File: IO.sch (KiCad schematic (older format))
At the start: 22 parts, among them SW2 CH1_Vadj, SW3 CH2_Vadj, U5 74HC14, U6 MCP23008-xP, U7 4013

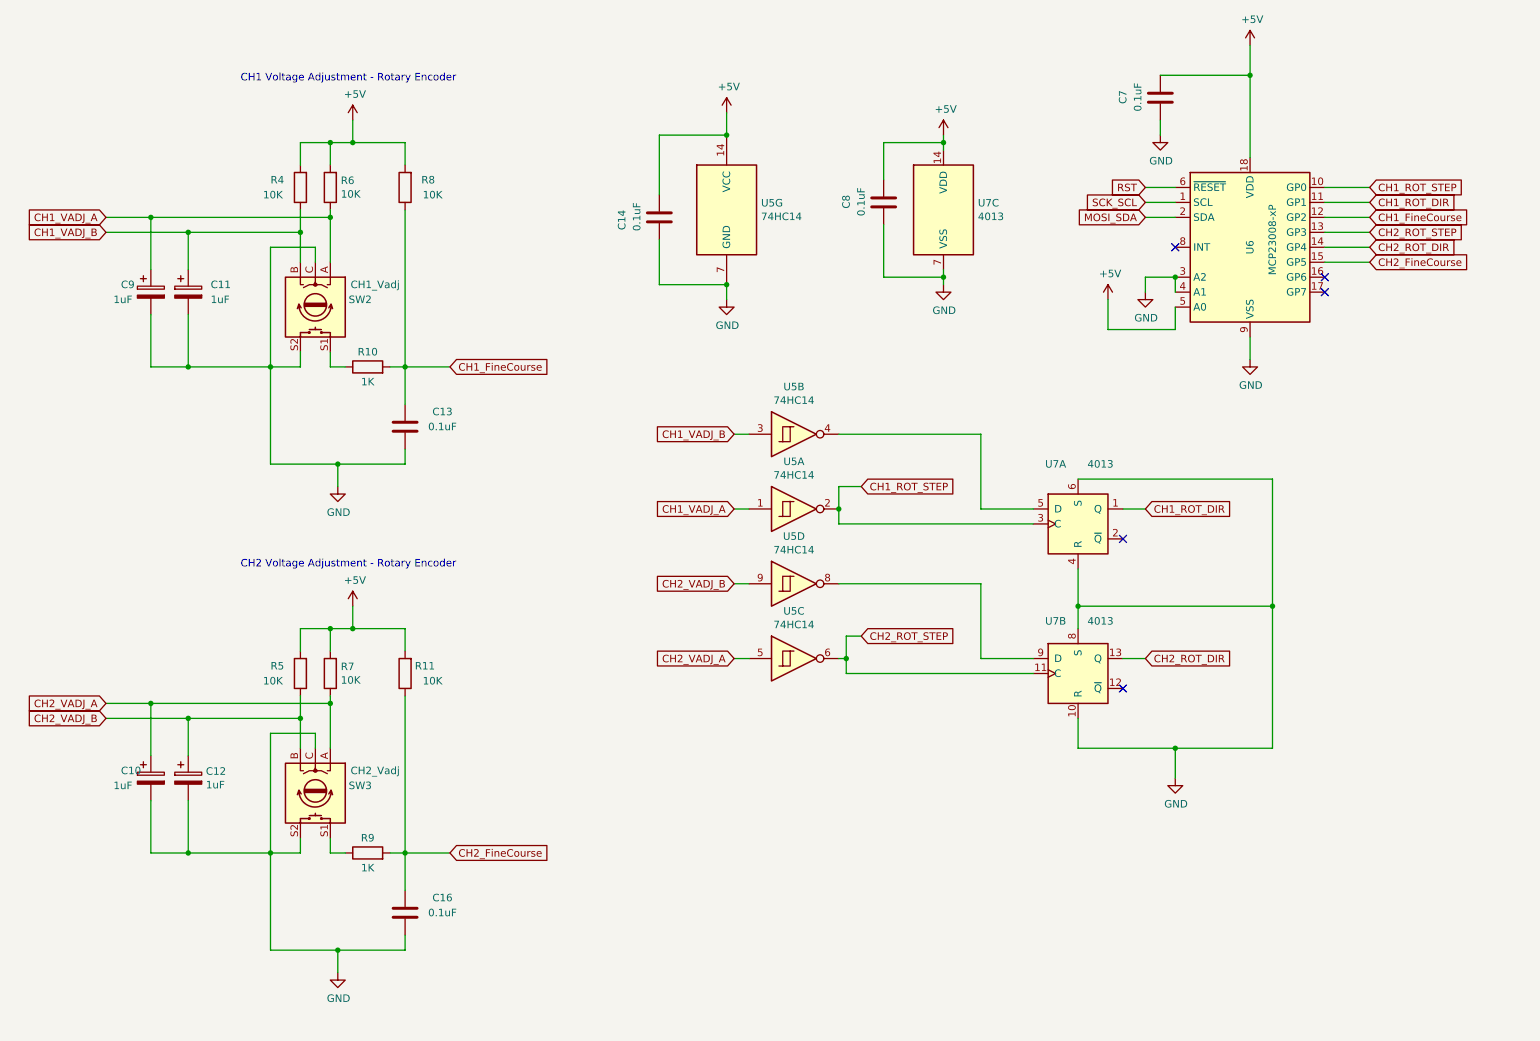
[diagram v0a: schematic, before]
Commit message: Switched the MCU to a basic STM32, changed the business logic to 3V3, created a new 3V3 regulator for this. Also initialised code base. We'll use ARM Mbed for rapid development
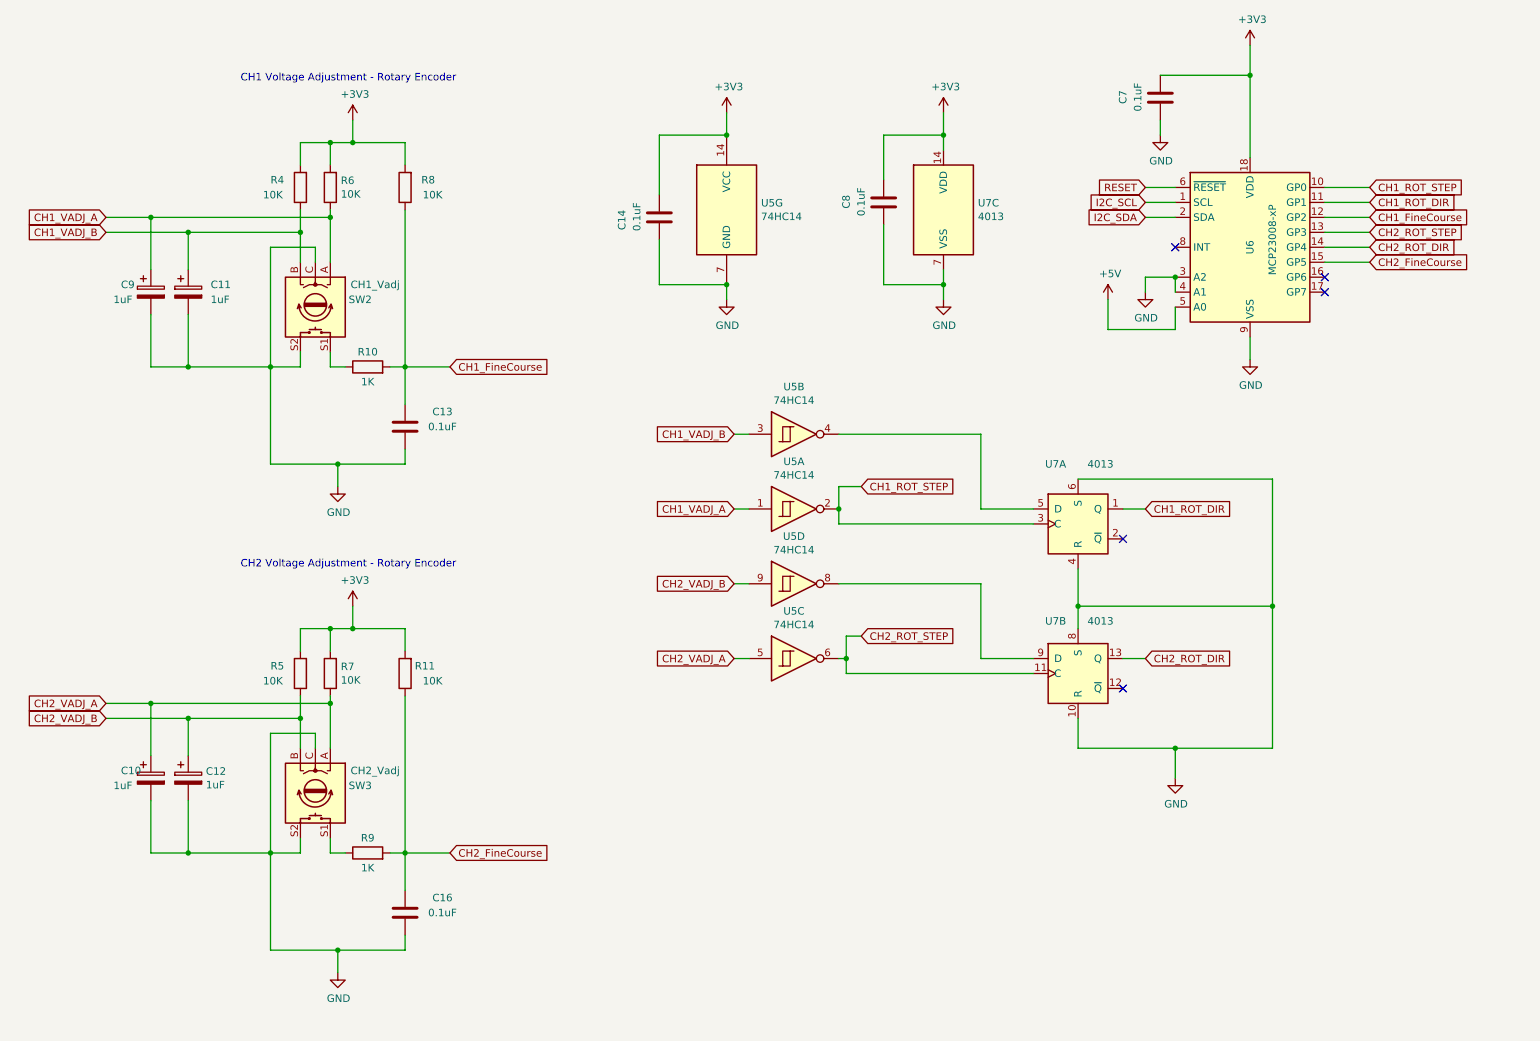
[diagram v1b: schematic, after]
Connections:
- net +5V: no longer C14.2, C7.2, C8.2, R11.2, R4.2, R5.2, R6.2, R7.2, R8.2, U5.14 (VCC), U6.18 (VDD), U7.14 (VDD)
- net MOSI_SDA renamed I2C_SDA
- net RST renamed RESET
- net SCK_SCL renamed I2C_SCL
- new net +3V3: C14.2, C7.2, C8.2, R11.2, R4.2, R5.2, R6.2, R7.2, R8.2, U5.14 (VCC), U6.18 (VDD), U7.14 (VDD)
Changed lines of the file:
@@
 	1    0    0    -1
 $EndComp
-Text GLabel 8300 1850 0    50   Input ~ 0
-RST
 Wire Wire Line
 	8500 1850 8300 1850
-Text GLabel 8300 1950 0    50   Input ~ 0
-SCK_SCL
-Text GLabel 8300 2050 0    50   Input ~ 0
-MOSI_SDA
 Wire Wire Line
 	8500 1950 8300 1950
@@
 	9000 1100 9000 900
 Connection ~ 9000 1100
-$Comp
-L power:+5V #PWR?
-U 1 1 60565429
-P 9000 900
-AR Path="/60565429" Ref="#PWR?"  Part="1"
-AR Path="/604E5285/60565429" Ref="#PWR0119"  Part="1"
-F 0 "#PWR0119" H 9000 750 50  0001 C CNN
-F 1 "+5V" H 9015 1073 50  0000 C CNN
-F 2 "" H 9000 900 50  0001 C CNN
-F 3 "" H 9000 900 50  0001 C CNN
-	1    9000 900
-	1    0    0    -1
-$EndComp
 Wire Wire Line
 	9500 1850 9800 1850
@@
 Wire Wire Line
 	9500 2350 9800 2350
-$Comp
-L power:+5V #PWR?
-U 1 1 605B59EA
-P 3000 1400
-AR Path="/605B59EA" Ref="#PWR?"  Part="1"
-AR Path="/604E5285/605B59EA" Ref="#PWR0121"  Part="1"
-F 0 "#PWR0121" H 3000 1250 50  0001 C CNN
-F 1 "+5V" H 3015 1573 50  0000 C CNN
-F 2 "" H 3000 1400 50  0001 C CNN
-F 3 "" H 3000 1400 50  0001 C CNN
-	1    3000 1400
-	1    0    0    -1
-$EndComp
 $Comp
 L Device:R R?
@@
 	1    0    0    -1
 $EndComp
-$Comp
-L 4xxx:4013 U?
-U 3 1 605B5AC9
-P 6950 2000
-AR Path="/605B5AC9" Ref="U?"  Part="3"
-AR Path="/604E5285/605B5AC9" Ref="U7"  Part="3"
-F 0 "U7" H 7180 2046 50  0000 L CNN
-F 1 "4013" H 7180 1955 50  0000 L CNN
-F 2 "" H 6950 2000 50  0001 C CNN
-F 3 "http://www.onsemi.com/pub/Collateral/MC14013B-D.PDF" H 6950 2000 50  0001 C CNN
-	3    6950 2000
-	1    0    0    -1
-$EndComp
 Text Notes 2250 1150 0    50   ~ 0
 CH1 Voltage Adjustment - Rotary Encoder\n
 $Comp
-L power:+5V #PWR?
-U 1 1 605B5AD1
-P 6950 1500
-AR Path="/605B5AD1" Ref="#PWR?"  Part="1"
-AR Path="/604E5285/605B5AD1" Ref="#PWR0124"  Part="1"
-F 0 "#PWR0124" H 6950 1350 50  0001 C CNN
-F 1 "+5V" H 6965 1673 50  0000 C CNN
-F 2 "" H 6950 1500 50  0001 C CNN
-F 3 "" H 6950 1500 50  0001 C CNN
-	1    6950 1500
-	1    0    0    -1
-$EndComp
-Wire Wire Line
-	6950 1500 6950 1550
-$Comp
 L power:GND #PWR?
 U 1 1 605B5AD8
-P 6950 2500
+P 6950 2600
 AR Path="/605B5AD8" Ref="#PWR?"  Part="1"
 AR Path="/604E5285/605B5AD8" Ref="#PWR0125"  Part="1"
-F 0 "#PWR0125" H 6950 2250 50  0001 C CNN
-F 1 "GND" H 6955 2327 50  0000 C CNN
-F 2 "" H 6950 2500 50  0001 C CNN
-F 3 "" H 6950 2500 50  0001 C CNN
-	1    6950 2500
-	1    0    0    -1
-$EndComp
-Wire Wire Line
-	6950 2400 6950 2450
+F 0 "#PWR0125" H 6950 2350 50  0001 C CNN
+F 1 "GND" H 6955 2427 50  0000 C CNN
+F 2 "" H 6950 2600 50  0001 C CNN
+F 3 "" H 6950 2600 50  0001 C CNN
+	1    6950 2600
+	1    0    0    -1
+$EndComp
 $Comp
 L Device:C C?
@@
 	-1   0    0    1
 $EndComp
-Wire Wire Line
-	6550 1550 6950 1550
-Connection ~ 6950 1550
-Wire Wire Line
-	6950 1550 6950 1600
-Wire Wire Line
-	6550 2450 6950 2450
-Connection ~ 6950 2450
-Wire Wire Line
-	6950 2450 6950 2500
-Wire Wire Line
-	6550 1800 6550 1550
-Wire Wire Line
-	6550 2100 6550 2450
 $Comp
 L 74xx:74HC14 U?
@@
 Wire Wire Line
 	2850 1550 3000 1550
-Wire Wire Line
-	3000 1550 3000 1400
 Connection ~ 3000 1550
 Wire Wire Line
@@
 Text GLabel 1350 2150 0    50   Input ~ 0
 CH1_VADJ_B
-$Comp
-L power:+5V #PWR?
-U 1 1 606CCC08
-P 3000 4650
-AR Path="/606CCC08" Ref="#PWR?"  Part="1"
-AR Path="/604E5285/606CCC08" Ref="#PWR04"  Part="1"
-F 0 "#PWR04" H 3000 4500 50  0001 C CNN
-F 1 "+5V" H 3015 4823 50  0000 C CNN
-F 2 "" H 3000 4650 50  0001 C CNN
-F 3 "" H 3000 4650 50  0001 C CNN
-	1    3000 4650
-	1    0    0    -1
-$EndComp
 $Comp
 L Device:R R?
@@
 	1    5050 2050
 	-1   0    0    1
-$EndComp
-$Comp
-L power:+5V #PWR?
-U 1 1 60790073
-P 5500 1350
-AR Path="/60790073" Ref="#PWR?"  Part="1"
-AR Path="/604E5285/60790073" Ref="#PWR09"  Part="1"
-F 0 "#PWR09" H 5500 1200 50  0001 C CNN
-F 1 "+5V" H 5515 1523 50  0000 C CNN
-F 2 "" H 5500 1350 50  0001 C CNN
-F 3 "" H 5500 1350 50  0001 C CNN
-	1    5500 1350
-	1    0    0    -1
 $EndComp
 $Comp
@@
 NoConn ~ 9500 2450
 NoConn ~ 9500 2550
+Text GLabel 8300 1950 0    50   Input ~ 0
+I2C_SCL
+Text GLabel 8300 2050 0    50   Input ~ 0
+I2C_SDA
+Text GLabel 8300 1850 0    50   Input ~ 0
+RESET
+$Comp
+L power:+3V3 #PWR?
+U 1 1 600ABCA0
+P 6950 1350
+F 0 "#PWR?" H 6950 1200 50  0001 C CNN
+F 1 "+3V3" H 6965 1523 50  0000 C CNN
+F 2 "" H 6950 1350 50  0001 C CNN
+F 3 "" H 6950 1350 50  0001 C CNN
+	1    6950 1350
+	1    0    0    -1
+$EndComp
+Wire Wire Line
+	6950 1500 6550 1500
+Wire Wire Line
+	6950 1350 6950 1500
+Wire Wire Line
+	6550 1500 6550 1800
+$Comp
+L 4xxx:4013 U?
+U 3 1 605B5AC9
+P 6950 2000
+AR Path="/605B5AC9" Ref="U?"  Part="3"
+AR Path="/604E5285/605B5AC9" Ref="U7"  Part="3"
+F 0 "U7" H 7180 2046 50  0000 L CNN
+F 1 "4013" H 7180 1955 50  0000 L CNN
+F 2 "" H 6950 2000 50  0001 C CNN
+F 3 "http://www.onsemi.com/pub/Collateral/MC14013B-D.PDF" H 6950 2000 50  0001 C CNN
+	3    6950 2000
+	1    0    0    -1
+$EndComp
+Wire Wire Line
+	6950 1600 6950 1500
+Connection ~ 6950 1500
+Wire Wire Line
+	6950 2400 6950 2500
+Wire Wire Line
+	6550 2500 6950 2500
+Wire Wire Line
+	6550 2100 6550 2500
+Connection ~ 6950 2500
+Wire Wire Line
+	6950 2500 6950 2600
+Wire Wire Line
+	3000 1550 3000 1400
+$Comp
+L power:+3V3 #PWR?
+U 1 1 600C9E7A
+P 3000 1400
+F 0 "#PWR?" H 3000 1250 50  0001 C CNN
+F 1 "+3V3" H 3015 1573 50  0000 C CNN
+F 2 "" H 3000 1400 50  0001 C CNN
+F 3 "" H 3000 1400 50  0001 C CNN
+	1    3000 1400
+	1    0    0    -1
+$EndComp
+$Comp
+L power:+3V3 #PWR?
+U 1 1 600CA50D
+P 5500 1350
+F 0 "#PWR?" H 5500 1200 50  0001 C CNN
+F 1 "+3V3" H 5515 1523 50  0000 C CNN
+F 2 "" H 5500 1350 50  0001 C CNN
+F 3 "" H 5500 1350 50  0001 C CNN
+	1    5500 1350
+	1    0    0    -1
+$EndComp
+$Comp
+L power:+3V3 #PWR?
+U 1 1 600CB0A8
+P 9000 900
+F 0 "#PWR?" H 9000 750 50  0001 C CNN
+F 1 "+3V3" H 9015 1073 50  0000 C CNN
+F 2 "" H 9000 900 50  0001 C CNN
+F 3 "" H 9000 900 50  0001 C CNN
+	1    9000 900
+	1    0    0    -1
+$EndComp
+$Comp
+L power:+3V3 #PWR?
+U 1 1 600CB5E9
+P 3000 4650
+F 0 "#PWR?" H 3000 4500 50  0001 C CNN
+F 1 "+3V3" H 3015 4823 50  0000 C CNN
+F 2 "" H 3000 4650 50  0001 C CNN
+F 3 "" H 3000 4650 50  0001 C CNN
+	1    3000 4650
+	1    0    0    -1
+$EndComp
 $EndSCHEMATC

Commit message: had to reload source files. Waiting on the STM32F01 so will compile for target STM32F303 for now. Just a temporary change for now
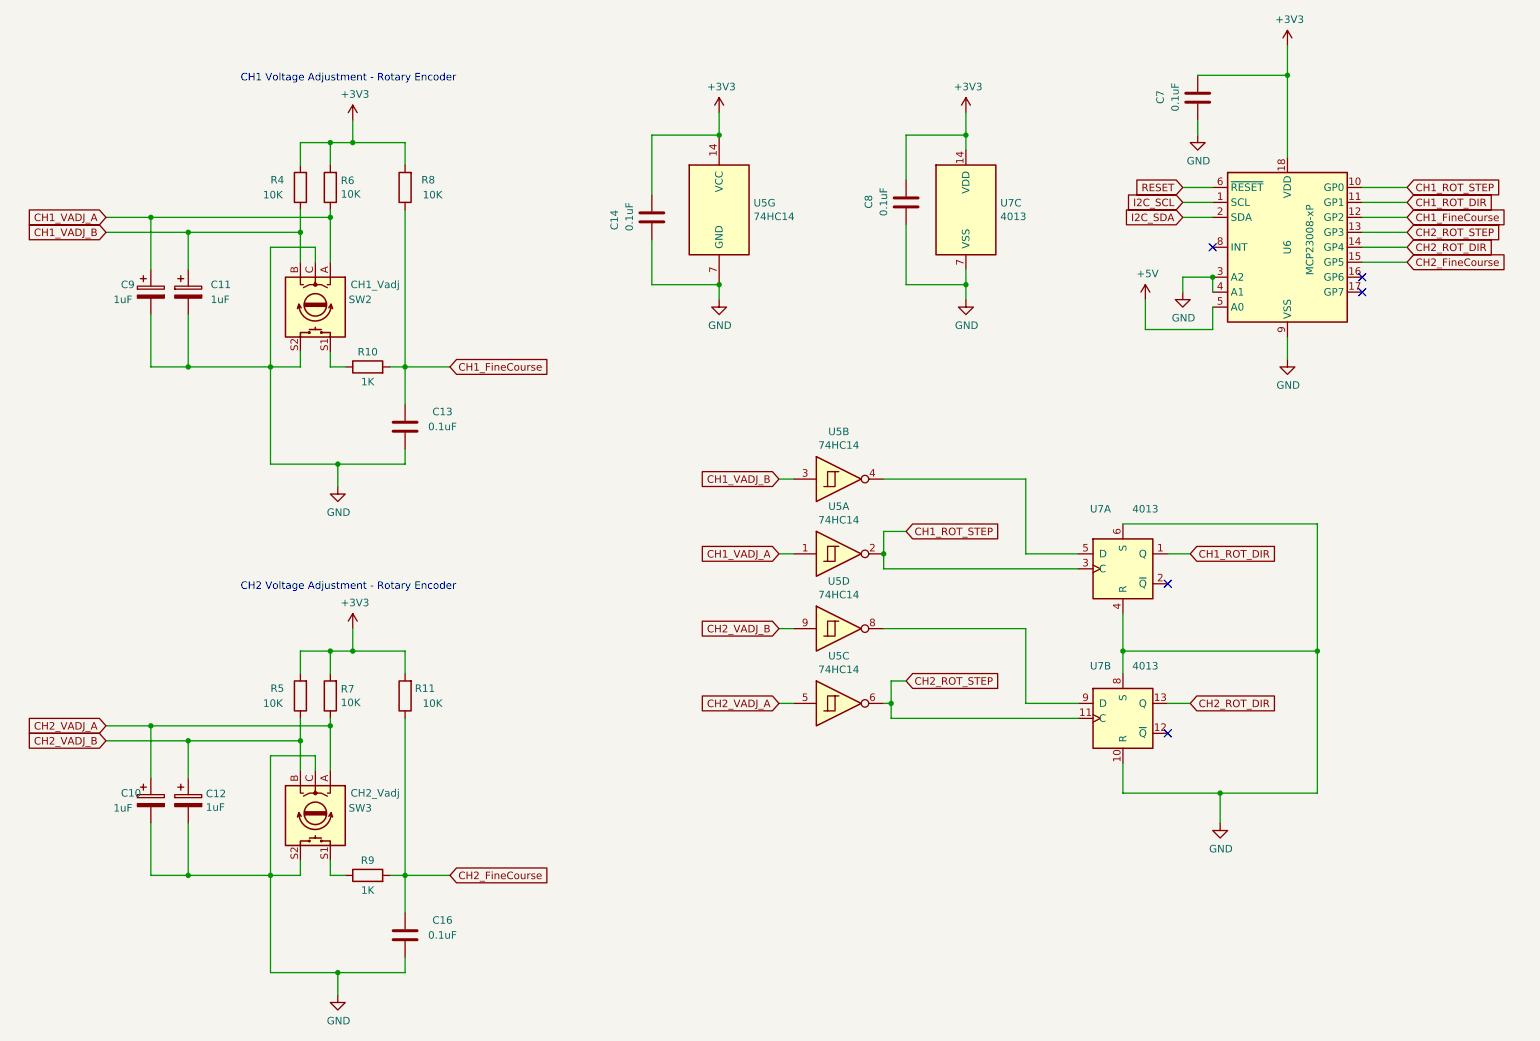
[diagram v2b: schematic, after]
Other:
- moved on the sheet: C10, C12, C14, C16, C7, C8, R11, R5, R7, R9, SW3, U5A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
